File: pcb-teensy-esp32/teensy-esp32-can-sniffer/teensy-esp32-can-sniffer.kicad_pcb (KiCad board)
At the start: 2 copper layers, 68.6 x 40.6 mm, 21 parts, among them J1 Conn_01x04, U1 Seeed_Studio_XIAO_ESP32S3, U2 Teensy4.0, U3 AP63205WU, U4 TJA1051T-3

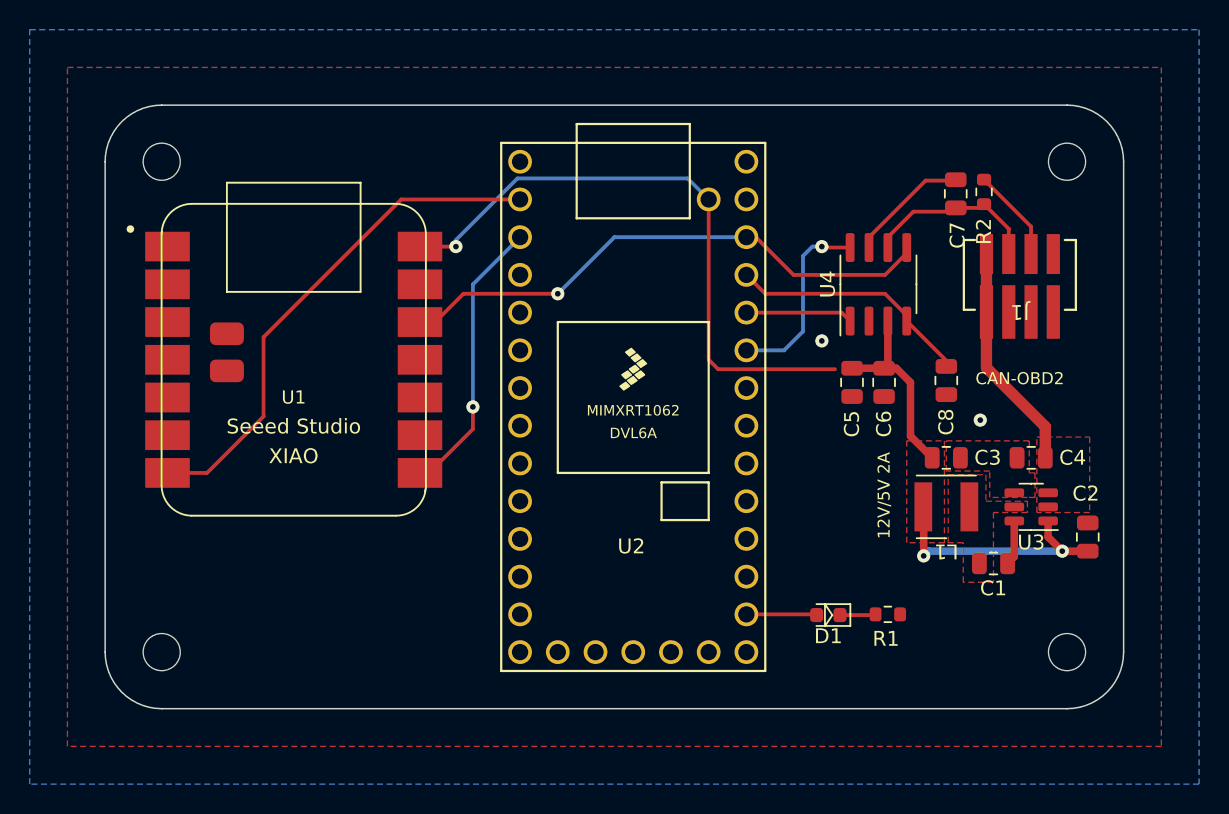
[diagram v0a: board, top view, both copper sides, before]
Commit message: Add UI labels and update PCB assets
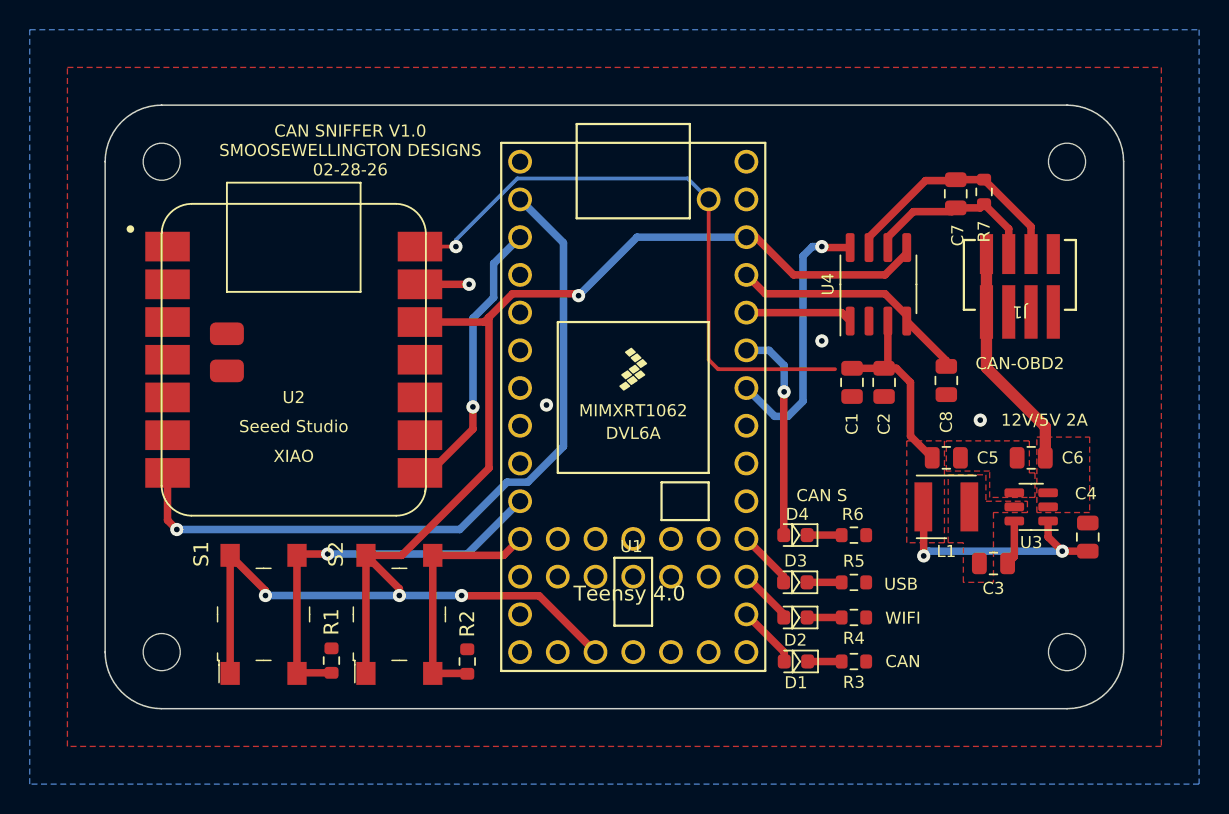
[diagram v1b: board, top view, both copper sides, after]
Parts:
- added D2: LED, LED_SMD:LED_0603_1608Metric, F.Cu at (71.9, 49.7)
- added D3: LED, LED_SMD:LED_0603_1608Metric, F.Cu at (71.9, 47.4)
- added D4: LED, LED_SMD:LED_0603_1608Metric, F.Cu at (71.9, 44.2)
- added R1: 10k, Resistor_SMD:R_0603_1608Metric, F.Cu at (40.6, 52.6)
- added R2: 10k, Resistor_SMD:R_0603_1608Metric, F.Cu at (49.8, 52.7)
- added R4: 330, Resistor_SMD:R_0603_1608Metric, F.Cu at (75.8, 49.7)
- added R5: 330, Resistor_SMD:R_0603_1608Metric, F.Cu at (75.8, 47.4)
- added R6: 330, Resistor_SMD:R_0603_1608Metric, F.Cu at (75.8, 44.2)
- added S1: PTS645SM43SMTR92_LFS, digikey-footprints:Switch_Tactile_SMD_6x6mm_PTS645, F.Cu at (36.1, 49.5)
- added S2: PTS645SM43SMTR92_LFS, digikey-footprints:Switch_Tactile_SMD_6x6mm_PTS645, F.Cu at (45.2, 49.5)
- L1: value L -> 4.7u
- moved R3 3.91 mm to (75.8, 52.7)
- moved D1 3.81 mm to (71.9, 52.7)
- renumbered C5 to C1, C6 to C2, C1 to C3, C2 to C4, C3 to C5, C4 to C6, R1 to R3, R2 to R7, U2 to U1, U1 to U2
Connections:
- net CAN_LED_STATUS renamed /CAN_HEARTBEAT
- U1 pad 10: unconnected-(U2-Pad10) (its old number) -> /BUTTON_MODE
- U1 pad 11: unconnected-(U2-Pad11) (its old number) -> /BUTTON_SELECT
- U1 pad 16: unconnected-(U2-Pad16) (its old number) -> +3V3
- U1 pad 22: unconnected-(U2-Pad22) -> /WIFI_HEARTBEAT
- U1 pad 23: unconnected-(U2-Pad23) -> /USB_HEARTBEAT
- U1 pad 27: unconnected-(U2-Pad27) -> CAN_SILENT
- U1 pad 28: CAN_SILENT -> /CAN_SILENT_STATUS
- U1 pad 33: unconnected-(U2-Pad33) -> +5V
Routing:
- net +3V3: track 37.2 -> 105.2 mm, vias 1 -> 4
- net /BUTTON_MODE: track 0.00 -> 26.8 mm, vias 0 -> 1
- net /BUTTON_SELECT: track 0.00 -> 16.6 mm
- net ESP_UART_TX: track 34.5 -> 50.3 mm, vias 0 -> 1
- net /CAN_SILENT_STATUS: track 0.00 -> 14.4 mm, vias 0 -> 1
- net CAN_SILENT: track 12.9 -> 18.3 mm
- net /USB_HEARTBEAT: track 0.00 -> 3.96 mm
- net /WIFI_HEARTBEAT: track 0.00 -> 3.79 mm
- net GND: track 0.00 -> 3.31 mm, vias 2 -> 4
- net Net-(D3-Pad1): track 0.00 -> 2.34 mm
- net Net-(D2-Pad1): track 0.00 -> 2.32 mm
- net Net-(D4-Pad1): track 0.00 -> 2.32 mm
- net CAN_H: track 14.5 -> 16.4 mm
- net /CAN_HEARTBEAT: track 4.75 -> 4.23 mm
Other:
- board text added: "CAN"
- board text added: "CAN S"
- board text added: "CAN SNIFFER V1.0 SMOOSEWELLINGTON DESIGNS 02-28-26"
- board text added: "Teensy 4.0"
- board text added: "USB"
- board text added: "WIFI"
